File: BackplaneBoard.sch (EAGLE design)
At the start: 1 part

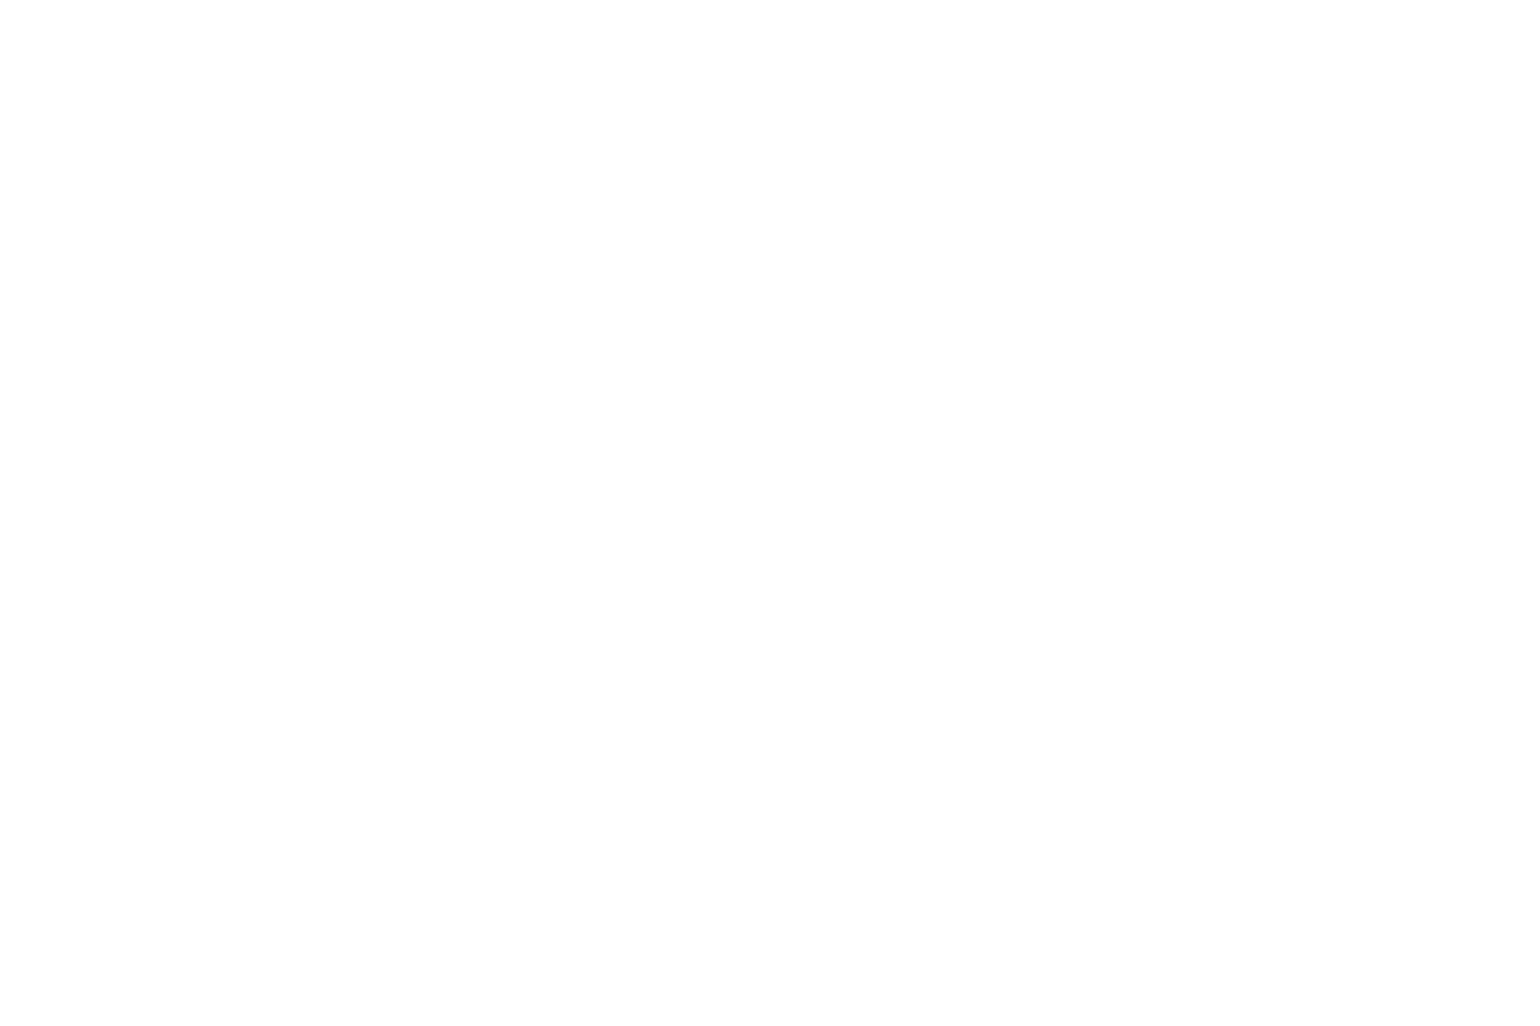
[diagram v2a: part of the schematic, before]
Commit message: added connectors
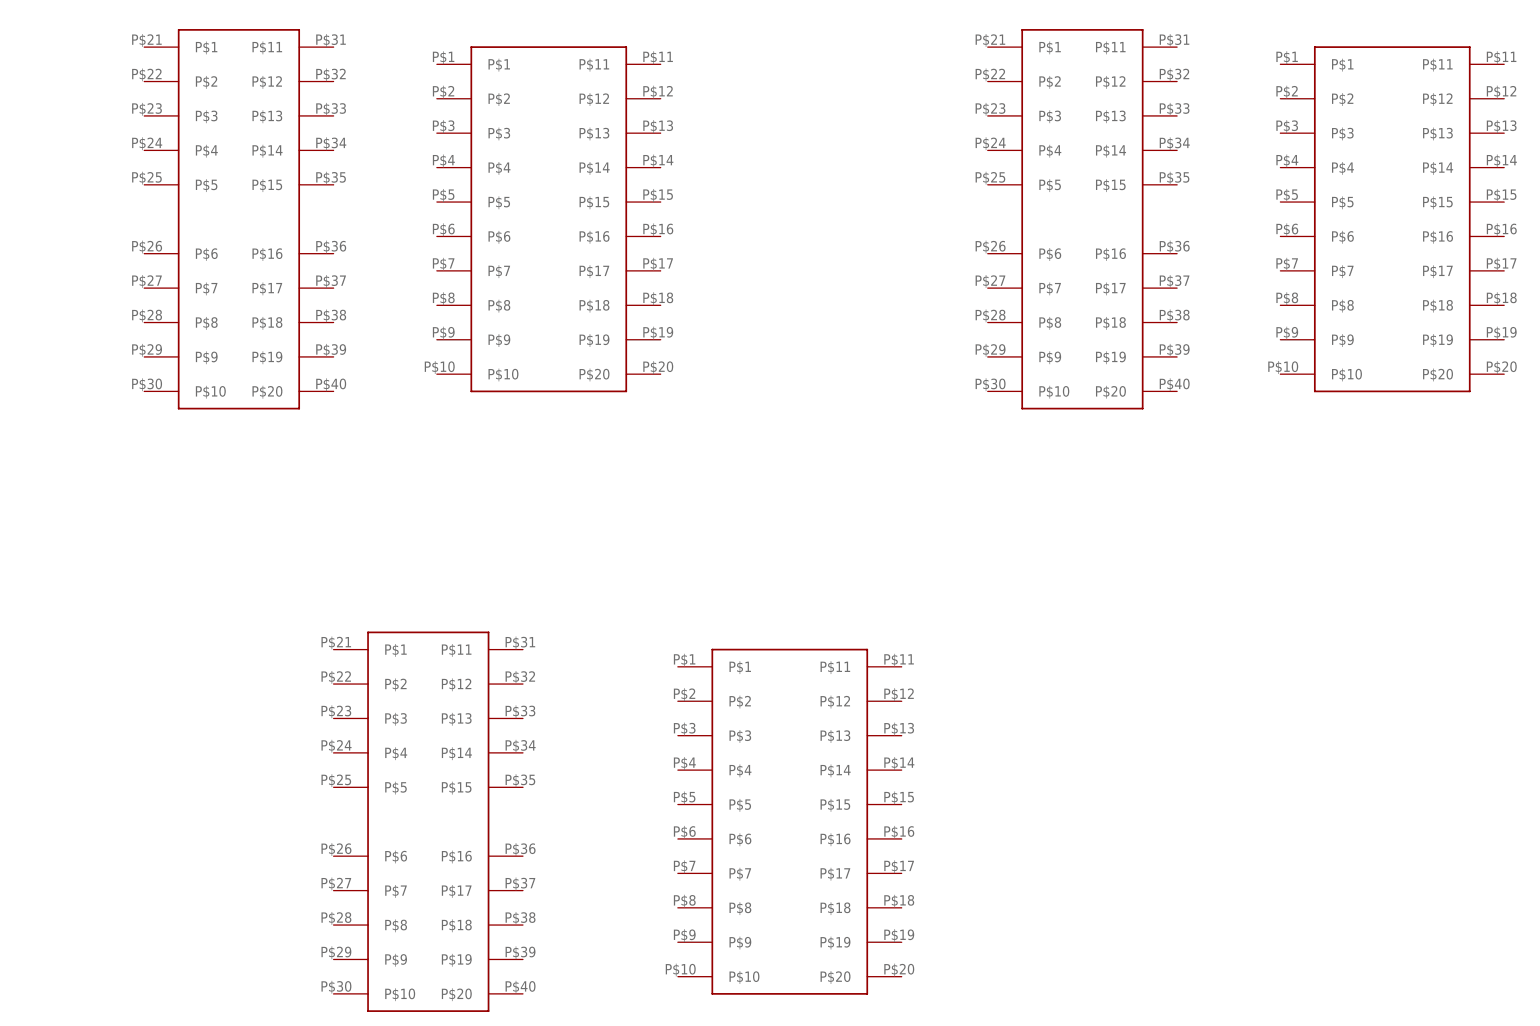
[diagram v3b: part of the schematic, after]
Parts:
- added U$2, U$3, U$4: ESC2BACKPLANE, ESC_to_Backplane_Connectors:ESC2BACKPLANE
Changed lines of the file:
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@@
 <?xml version="1.0" encoding="utf-8"?>
 <!DOCTYPE eagle SYSTEM "eagle.dtd">
-<eagle version="9.2.0">
+<eagle version="9.1.3">
 <drawing>
 <settings>
@@
 <part name="U$1" library="ET60S-02-24-02-X-VP-GP" deviceset="ET60S-02-24-02-X-VP-GP" device=""/>
 <part name="FRAME2" library="frames" library_urn="urn:adsk.eagle:library:229" deviceset="A4L-LOC" device=""/>
+<part name="U$2" library="ESC_to_Backplane_Connectors" deviceset="ESC2BACKPLANE" device=""/>
+<part name="U$3" library="ESC_to_Backplane_Connectors" deviceset="ESC2BACKPLANE" device=""/>
+<part name="U$4" library="ESC_to_Backplane_Connectors" deviceset="ESC2BACKPLANE" device=""/>
 </parts>
 <sheets>
@@
 <attribute name="SHEET" x="492.125" y="5.08" size="2.54" layer="94"/>
 </instance>
+<instance part="U$2" gate="G$1" x="289.56" y="134.62"/>
+<instance part="U$2" gate="G$2" x="335.28" y="137.16"/>
+<instance part="U$3" gate="G$1" x="414.02" y="134.62"/>
+<instance part="U$3" gate="G$2" x="459.74" y="137.16"/>
+<instance part="U$4" gate="G$1" x="317.5" y="45.72"/>
+<instance part="U$4" gate="G$2" x="370.84" y="48.26"/>
 </instances>
 <busses>

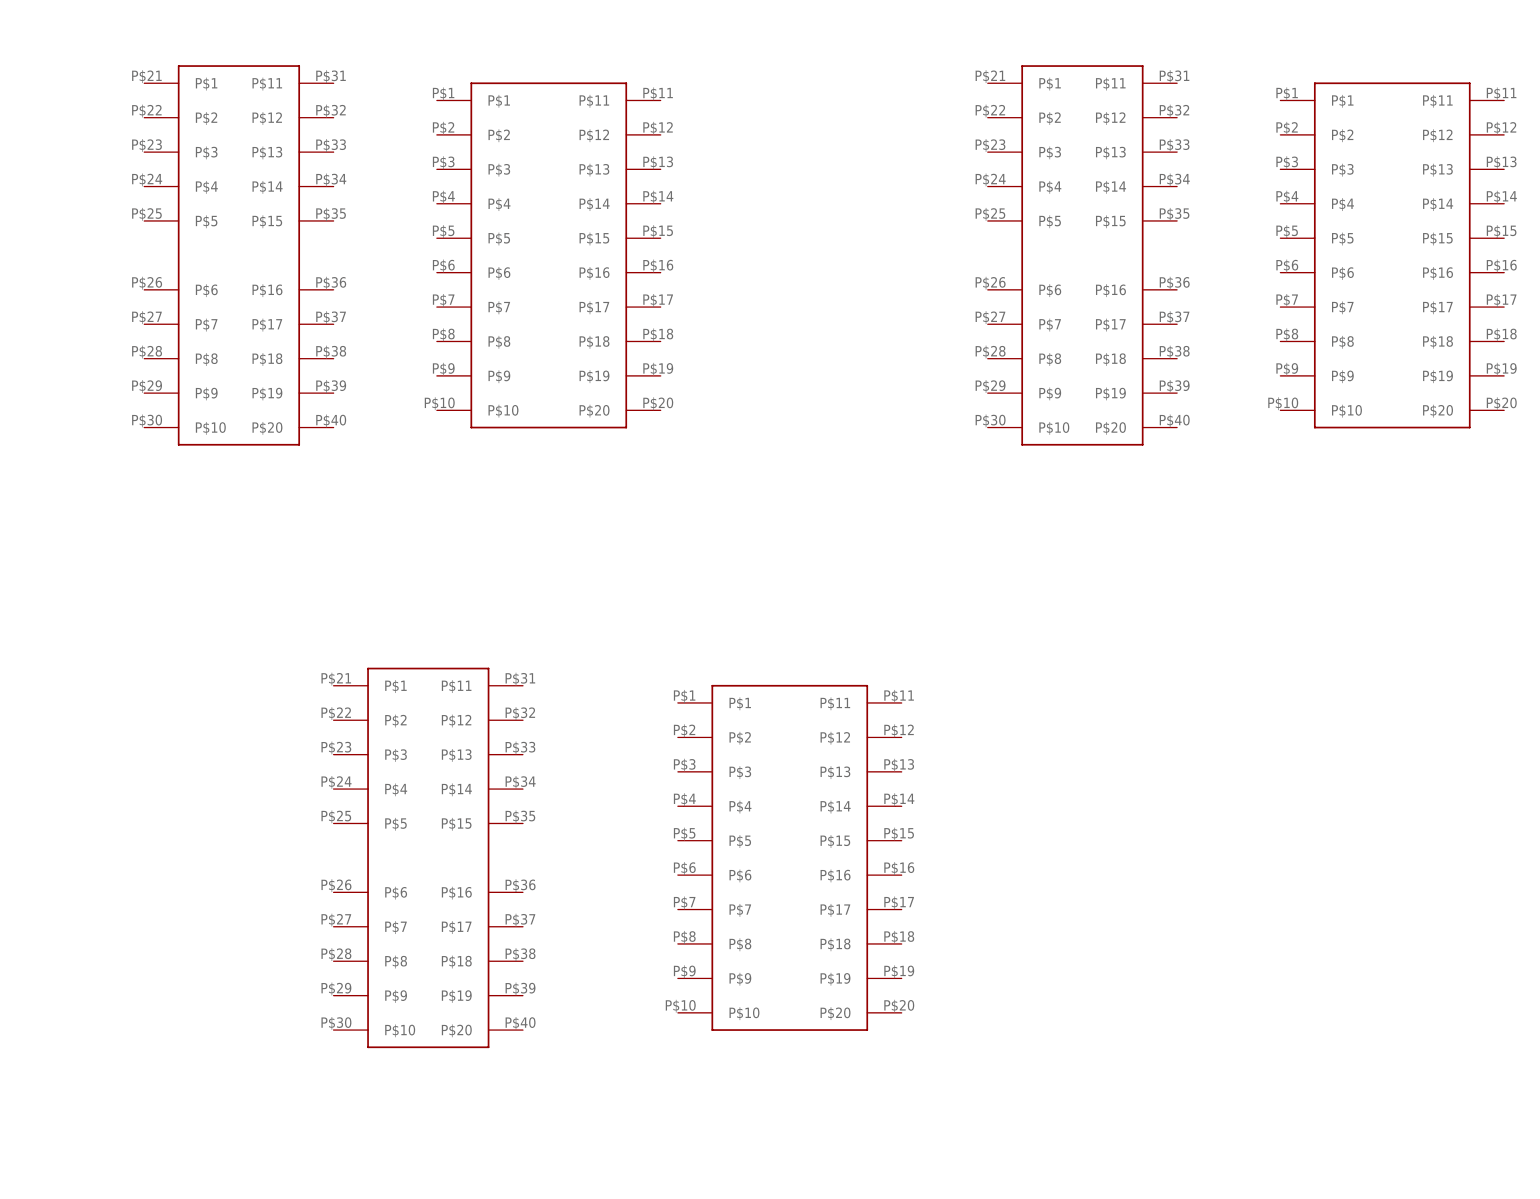
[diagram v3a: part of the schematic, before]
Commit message: updated connectors
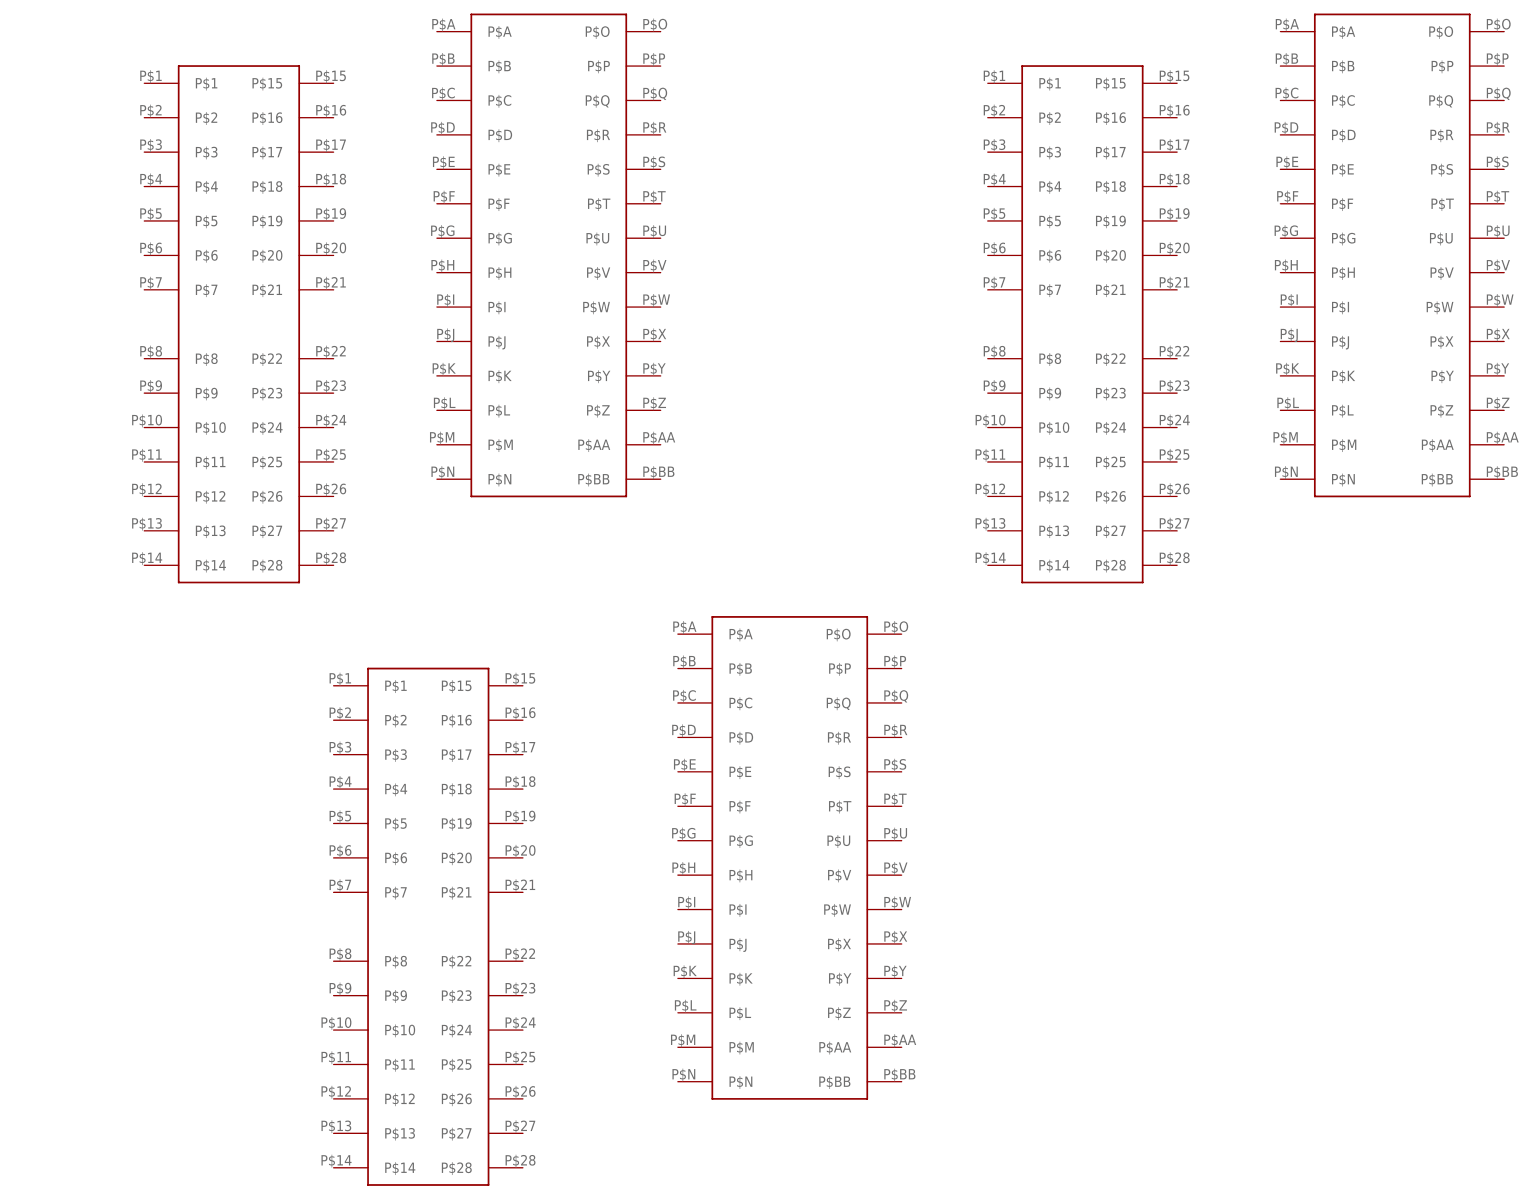
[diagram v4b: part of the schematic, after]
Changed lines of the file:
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@@
 <?xml version="1.0" encoding="utf-8"?>
 <!DOCTYPE eagle SYSTEM "eagle.dtd">
-<eagle version="9.1.3">
+<eagle version="9.2.0">
 <drawing>
 <settings>
